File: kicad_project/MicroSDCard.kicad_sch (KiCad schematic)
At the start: 7 parts, among them J8 DM3AT, U13 74LVC1G125

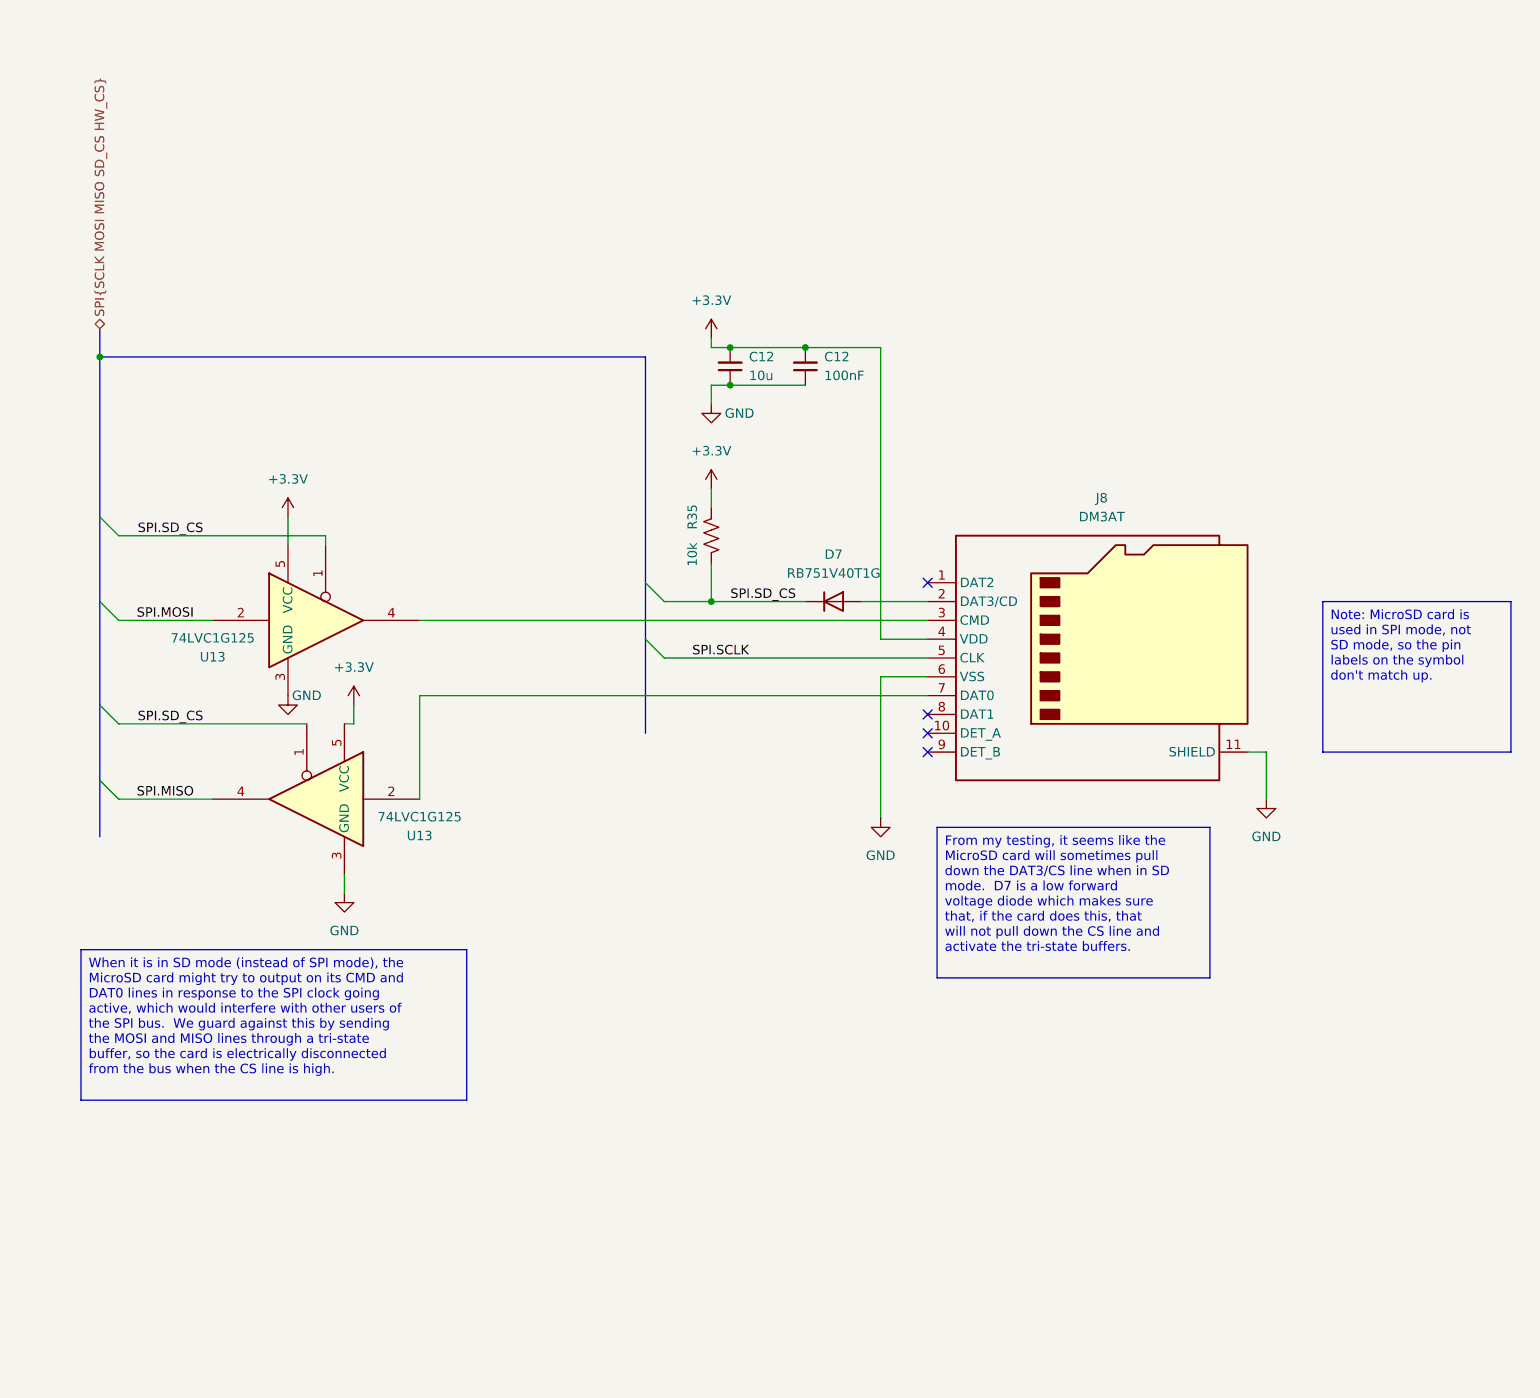
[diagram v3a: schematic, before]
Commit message: Start on SD card and usb-serial changes
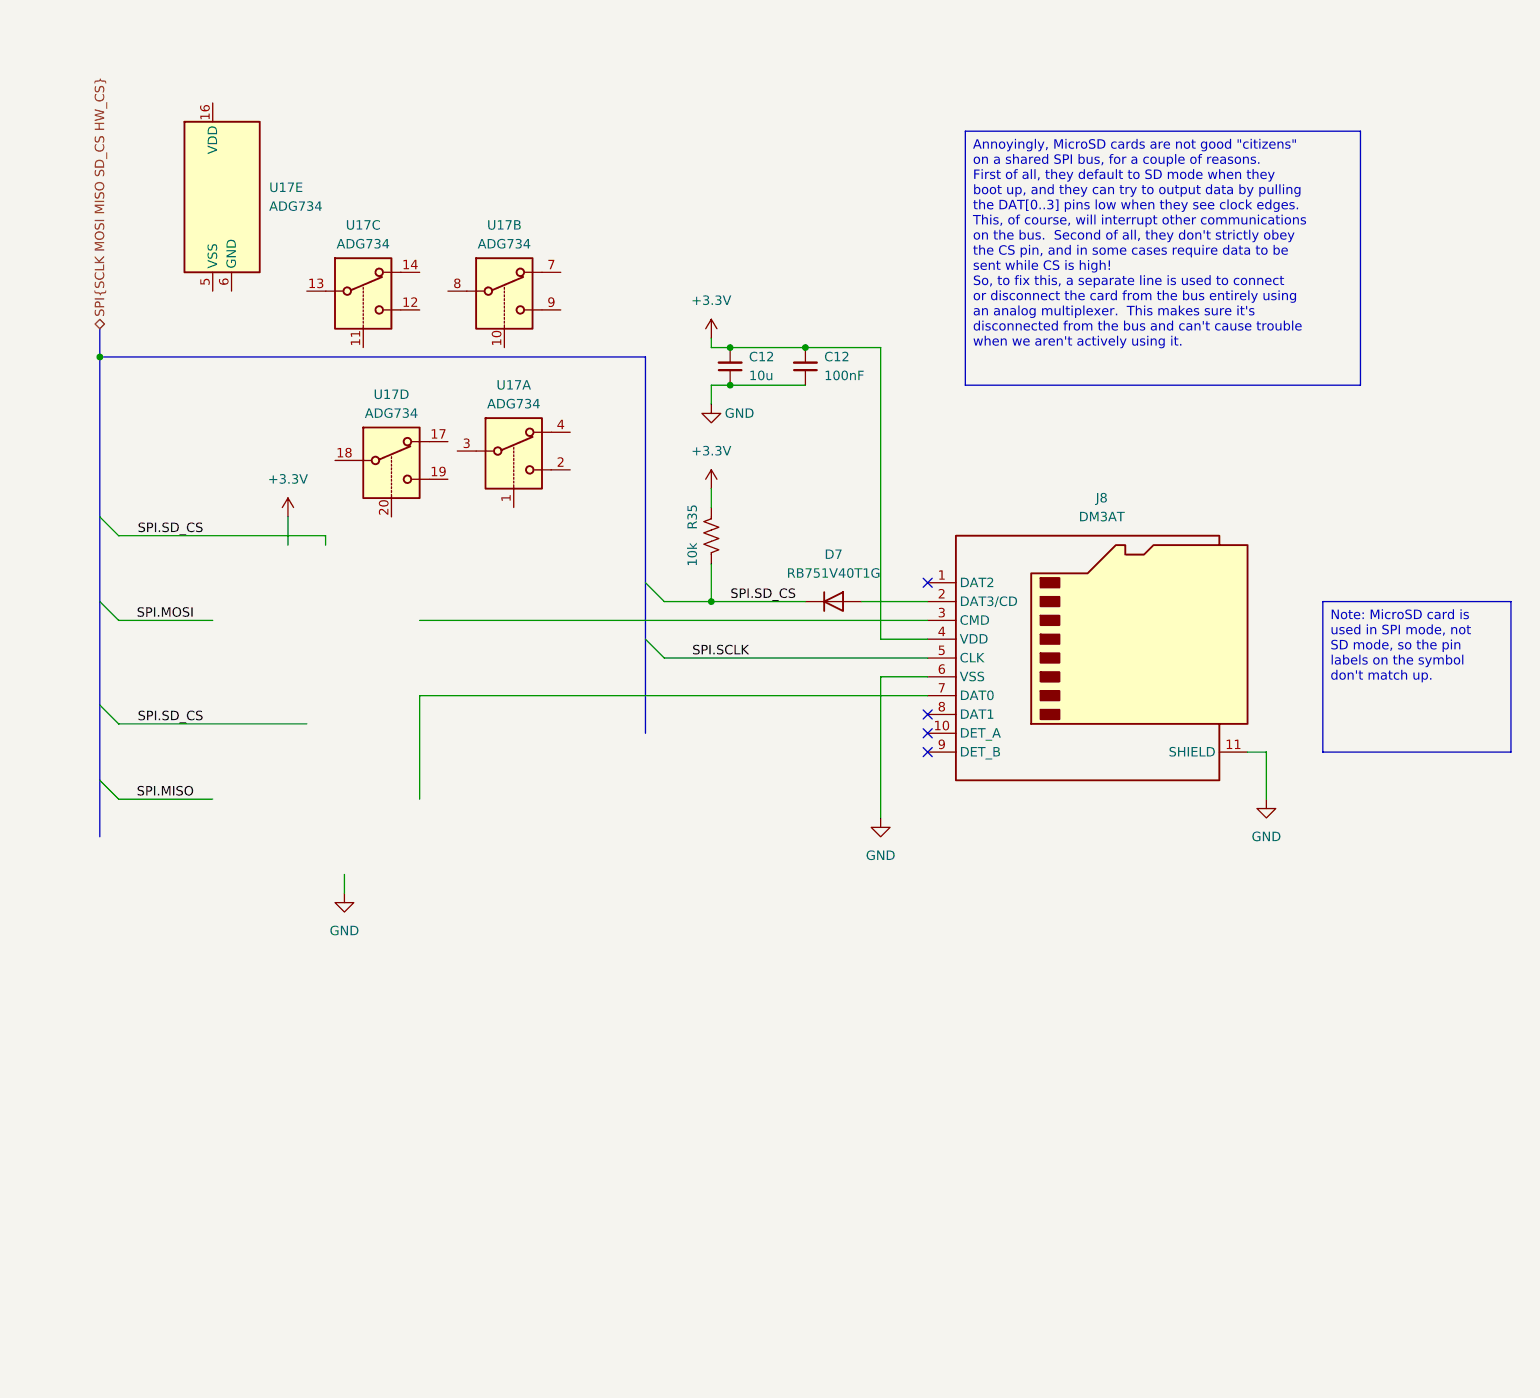
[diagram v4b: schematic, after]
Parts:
- removed U13 (x2): 74LVC1G125, project libraries:SOT-753, symbol 74xGxx:74LVC1G125
- added U17: ADG734, Package_SO:TSSOP-20_4.4x6.5mm_P0.65mm, symbol Analog_Switch:ADG734

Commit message: Update MicroSD card socket to have analog switch
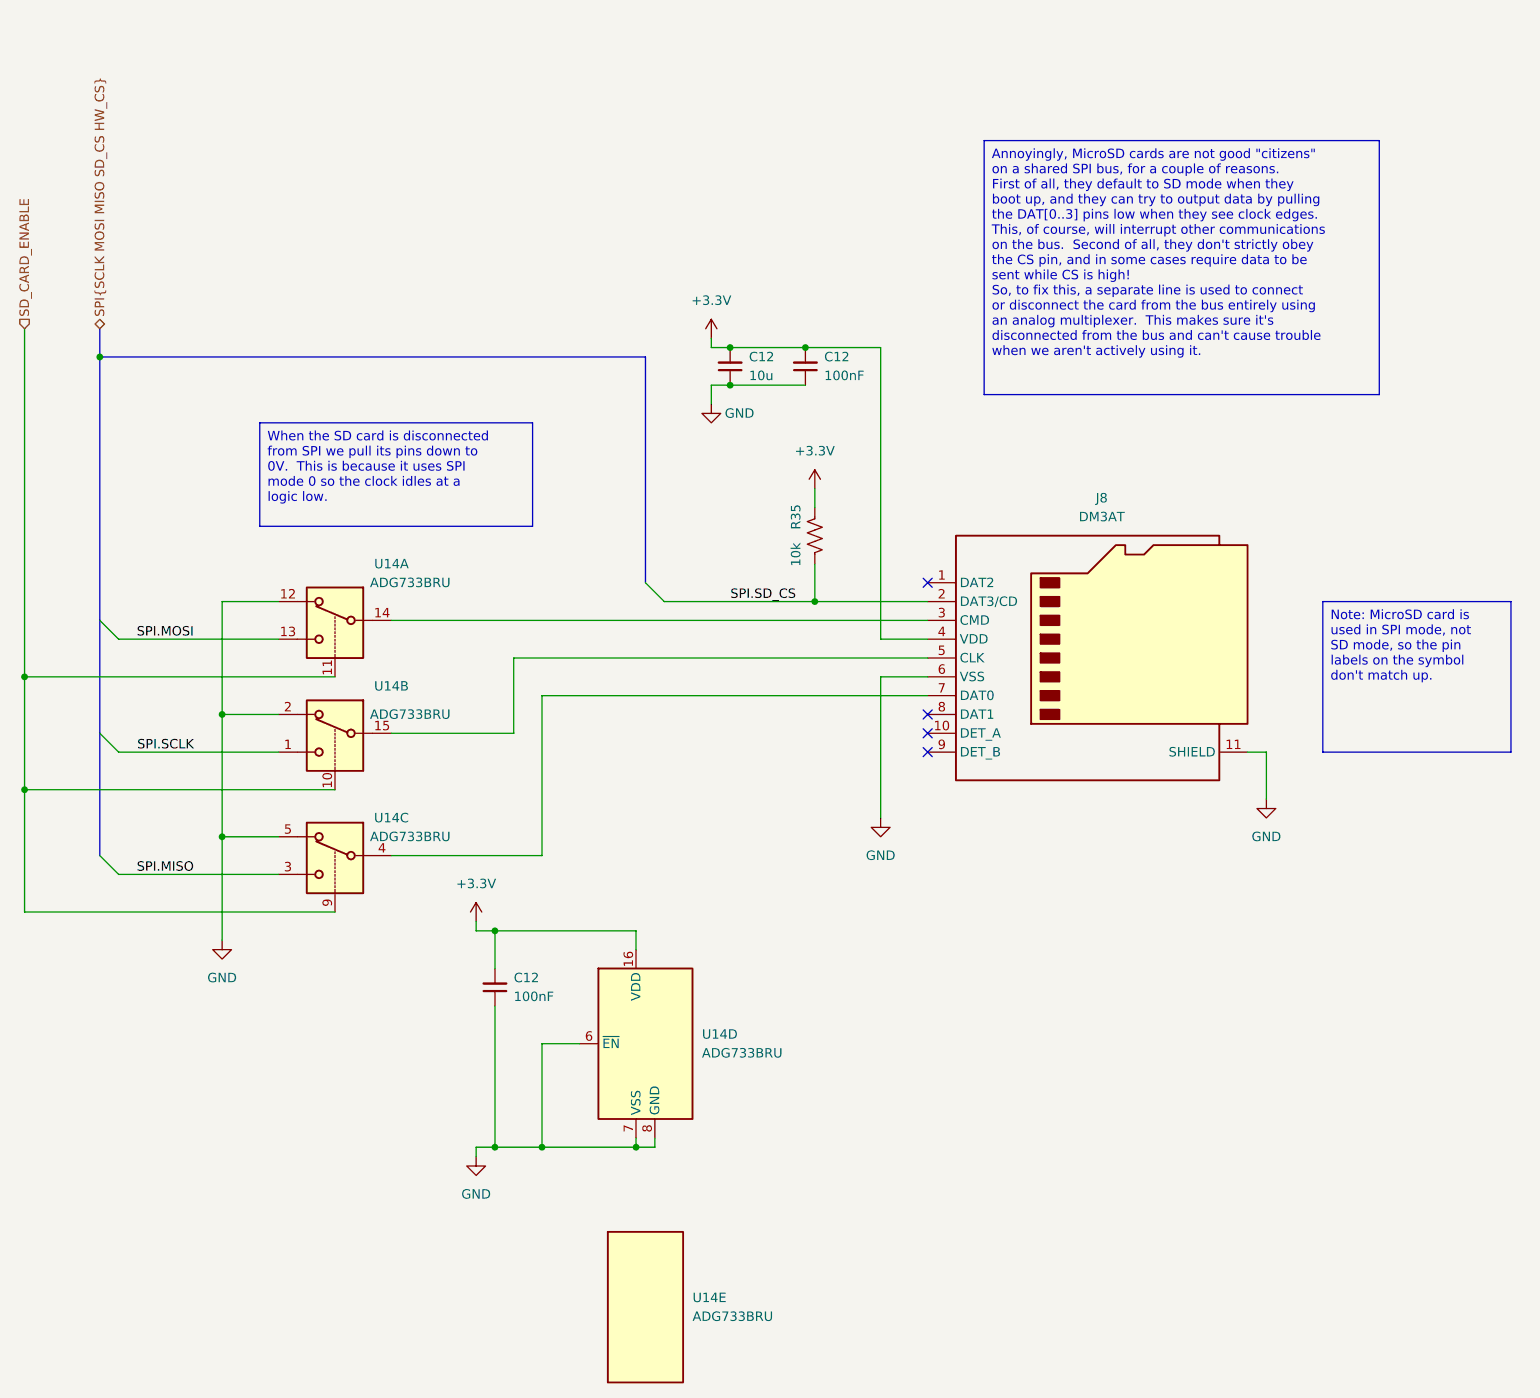
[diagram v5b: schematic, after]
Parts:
- removed D7: RB751V40T1G, Diode_SMD:D_SOD-323, symbol project libraries:RB751V40T1G
- removed U17: ADG734, Package_SO:TSSOP-20_4.4x6.5mm_P0.65mm, symbol Analog_Switch:ADG734
- added C12: 100nF, Capacitor_SMD:C_1206_3216Metric, symbol Device:C_Small
- added U14: ADG733BRU, project libraries:TSSOP-16_4.4x5mm_P0.65mm, symbol Analog_Switch:ADG733BRU
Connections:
- net +3.3V: now also C12.2, U14.16 (VDD)
- net GND: now also C12.1, U14.12, U14.2, U14.5, U14.6 (~{EN}), U14.7 (VSS), U14.8 (GND)
- net SPI.MISO: now also U14.3
- net SPI.MOSI: now also U14.13
- net SPI.SCLK: now also U14.1; no longer J8.5 (CLK)
- net SPI.SD_CS: now also J8.2 (DAT3/CD)
- net at J8.3 (CMD): now also U14.14
- net at J8.7 (DAT0): now also U14.4
- new net: J8.5 (CLK), U14.15
- new net SD_CARD_ENABLE: U14.10, U14.11, U14.9

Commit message: Friendship ended with FT232H, now CY7C652xx is my friend
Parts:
- U14: footprint project libraries:TSSOP-16_4.4x5mm_P0.65mm -> Package_SO:TSSOP-20_4.4x6.5mm_P0.65mm
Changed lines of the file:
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@@
       (effects (font (size 1.27 1.27)) (justify left))
     )
-    (property "Footprint" "project libraries:TSSOP-16_4.4x5mm_P0.65mm" (at 111.76 181.61 0)
+    (property "Footprint" "Package_SO:TSSOP-20_4.4x6.5mm_P0.65mm" (at 111.76 181.61 0)
       (effects (font (size 1.27 1.27)) hide)
     )
@@
       (effects (font (size 1.27 1.27)))
     )
-    (property "Footprint" "project libraries:TSSOP-16_4.4x5mm_P0.65mm" (at 71.12 86.36 0)
+    (property "Footprint" "Package_SO:TSSOP-20_4.4x6.5mm_P0.65mm" (at 71.12 86.36 0)
       (effects (font (size 1.27 1.27)) hide)
     )
@@
       (effects (font (size 1.27 1.27)))
     )
-    (property "Footprint" "project libraries:TSSOP-16_4.4x5mm_P0.65mm" (at 71.12 118.11 0)
+    (property "Footprint" "Package_SO:TSSOP-20_4.4x6.5mm_P0.65mm" (at 71.12 118.11 0)
       (effects (font (size 1.27 1.27)) hide)
     )
@@
       (effects (font (size 1.27 1.27)))
     )
-    (property "Footprint" "project libraries:TSSOP-16_4.4x5mm_P0.65mm" (at 71.12 101.6 0)
+    (property "Footprint" "Package_SO:TSSOP-20_4.4x6.5mm_P0.65mm" (at 71.12 101.6 0)
       (effects (font (size 1.27 1.27)) hide)
     )
@@
       (effects (font (size 1.27 1.27)) (justify left))
     )
-    (property "Footprint" "project libraries:TSSOP-16_4.4x5mm_P0.65mm" (at 111.76 146.05 0)
-      (effects (font (size 1.27 1.27)) hide)
-    )
+    (property "Footprint" "Package_SO:TSSOP-20_4.4x6.5mm_P0.65mm" (at 111.76 146.05 0)
+      (effects (font (size 1.27 1.27)) hide)
+    )

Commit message: Finish routing v2.r2
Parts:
- added C14: 1u, Capacitor_SMD:C_1206_3216Metric, symbol Device:C_Small
- added U6: BD2221G-LBTR, Package_TO_SOT_SMD:SOT-23-5, symbol project libraries:BD2221G-LBTR
- U14: footprint Package_SO:TSSOP-20_4.4x6.5mm_P0.65mm -> Package_SO:TSSOP-16_4.4x5mm_P0.65mm
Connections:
- net +3.3V: now also C14.2, U6.1 (VIN); no longer C12.2, C12.2, J8.4 (VDD)
- net GND: now also C14.1, U6.2 (GND)
- net SD_CARD_ENABLE: now also U6.3 (~EN)
- new net SD_CARD_VDD: C12.2, C12.2, J8.4 (VDD), U6.5 (VOUT)
- no-connect marks 4 -> 5
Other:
- moved on the sheet: C12

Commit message: Fix some missing suppliers, remove old sheet
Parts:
- U14: Supplier (none) -> Digi-Key
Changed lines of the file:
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@@
+      (effects (font (size 1.27 1.27)) hide)
+    )
+    (property "Supplier" "Digi-Key" (at 111.76 181.61 0)
       (effects (font (size 1.27 1.27)) hide)
     )
@@
       (effects (font (size 1.27 1.27)) hide)
     )
+    (property "Supplier" "Digi-Key" (at 71.12 86.36 0)
+      (effects (font (size 1.27 1.27)) hide)
+    )
     (pin "11")
     (pin "12")
@@
       (effects (font (size 1.27 1.27)) hide)
     )
+    (property "Supplier" "Digi-Key" (at 71.12 118.11 0)
+      (effects (font (size 1.27 1.27)) hide)
+    )
     (pin "11")
     (pin "12")
@@
       (effects (font (size 1.27 1.27)) hide)
     )
+    (property "Supplier" "Digi-Key" (at 71.12 101.6 0)
+      (effects (font (size 1.27 1.27)) hide)
+    )
     (pin "11")
     (pin "12")
@@
       (effects (font (size 1.27 1.27)) hide)
     )
+    (property "Supplier" "Digi-Key" (at 111.76 146.05 0)
+      (effects (font (size 1.27 1.27)) hide)
+    )
